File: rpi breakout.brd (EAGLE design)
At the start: 114 x 102.9 mm, 57 parts, among them IC1 PCA9505, J1 RASPBERRYPI-40-PIN-GPIO_PTH, U1 MAX11642EEG, U2 MAX11642EEG, U3 MAX11642EEG

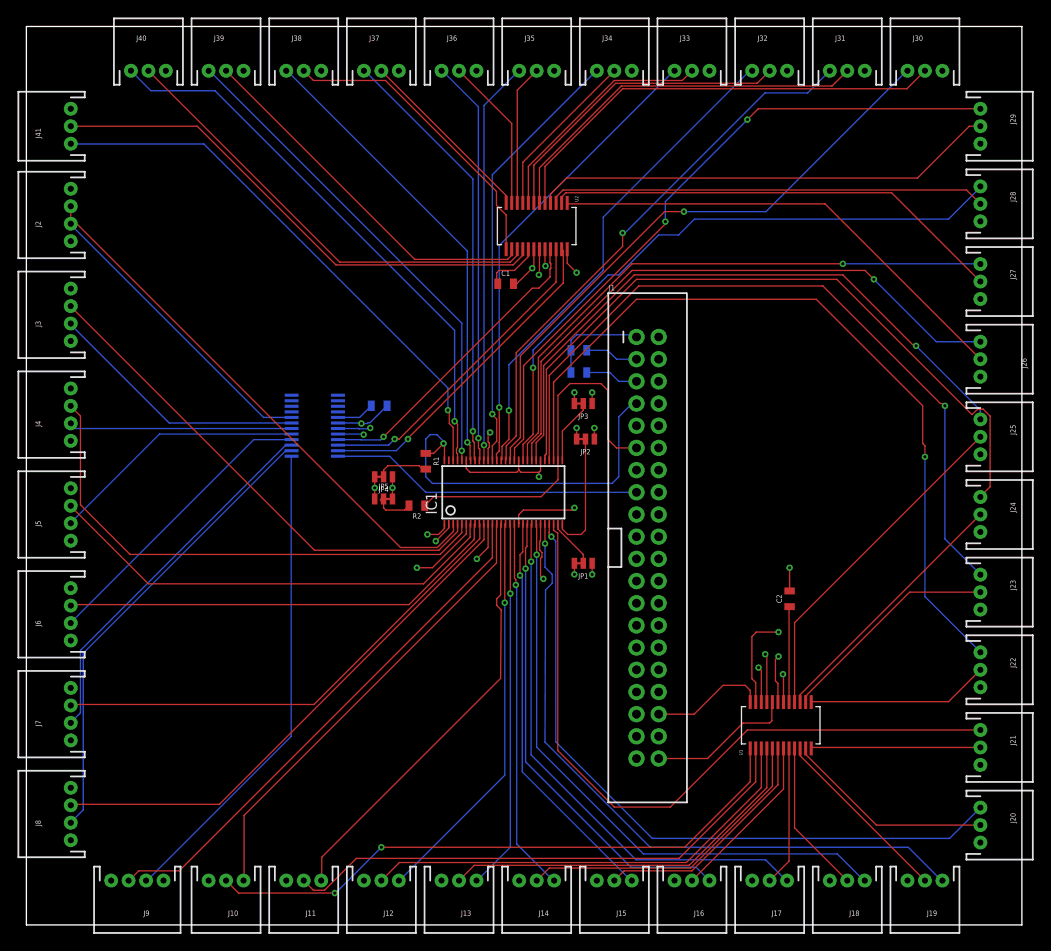
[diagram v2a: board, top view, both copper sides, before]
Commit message: updated silkscreen and increased trace sizes
increased sizes of all traces and update routing to clear DRC. Added silkscreen for all connections. Sent to fab
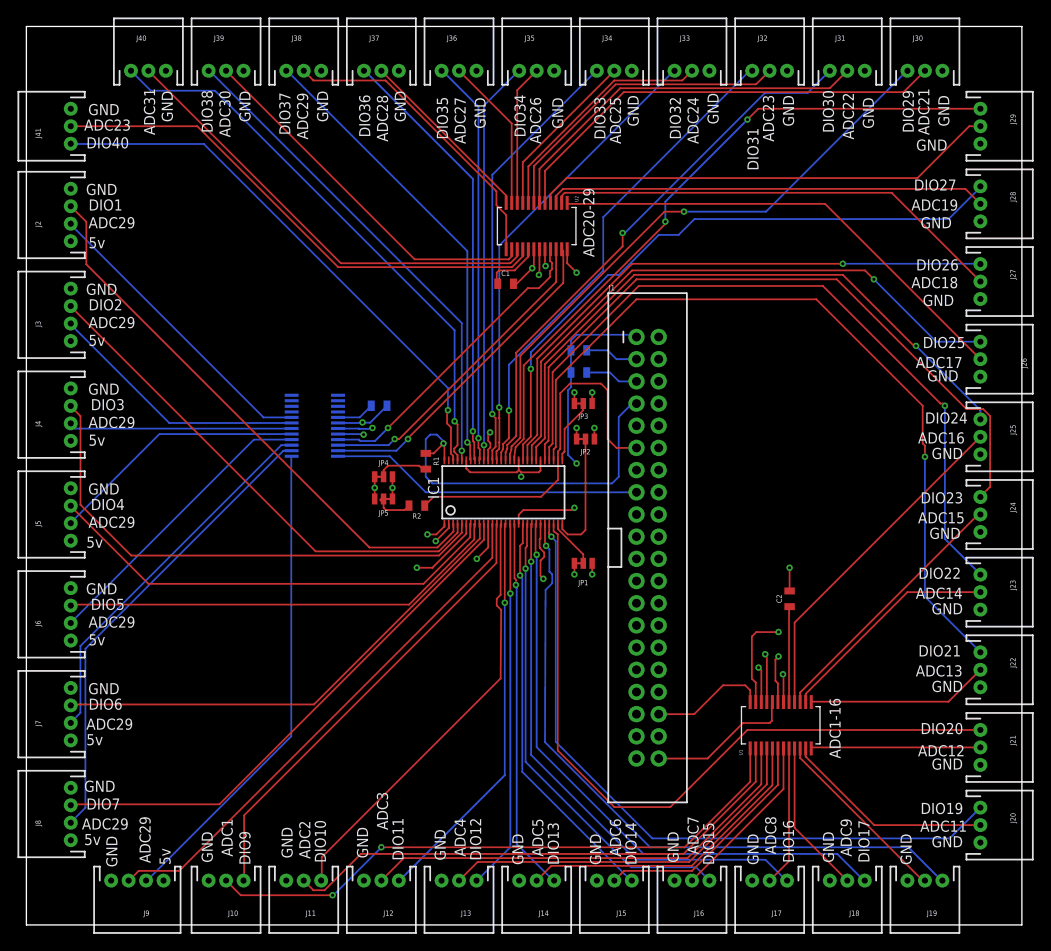
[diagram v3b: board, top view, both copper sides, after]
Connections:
- removed net 3.3V: J1.17
- net 3V: now also J1.17
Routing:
- net 3V: track 11.5 -> 31.8 mm, vias 0 -> 1
- net DIO1: track 62.4 -> 64.5 mm
- net DIO23: track 82.3 -> 81.8 mm
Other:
- board text added: "5v"
- board text added: "ADC1"
- board text added: "ADC1-16"
- board text added: "ADC11"
- board text added: "ADC12"
- board text added: "ADC13"
- board text added: "ADC14"
- board text added: "ADC15"
- board text added: "ADC16"
- board text added: "ADC17"
- board text added: "ADC18"
- board text added: "ADC19"
- board text added: "ADC2"
- board text added: "ADC20-29"
- board text added: "ADC21"
- board text added: "ADC22"
- board text added: "ADC23"
- board text added: "ADC24"
- board text added: "ADC25"
- board text added: "ADC26"
- board text added: "ADC27"
- board text added: "ADC28"
- board text added: "ADC29"
- board text added: "ADC3"
- board text added: "ADC30"
- board text added: "ADC31"
- board text added: "ADC33-39"
- board text added: "ADC4"
- board text added: "ADC5"
- board text added: "ADC6"
- board text added: "ADC7"
- board text added: "ADC8"
- board text added: "ADC9"
- board text added: "DIO1"
- board text added: "DIO10"
- board text added: "DIO11"
- board text added: "DIO12"
- board text added: "DIO13"
- board text added: "DIO14"
- board text added: "DIO15"
- board text added: "DIO16"
- board text added: "DIO17"
- board text added: "DIO19"
- board text added: "DIO2"
- board text added: "DIO20"
- board text added: "DIO21"
- board text added: "DIO22"
- board text added: "DIO23"
- board text added: "DIO24"
- board text added: "DIO25"
- board text added: "DIO26"
- board text added: "DIO27"
- board text added: "DIO29"
- board text added: "DIO3"
- board text added: "DIO30"
- board text added: "DIO31"
- board text added: "DIO32"
- board text added: "DIO33"
- board text added: "DIO34"
- board text added: "DIO35"
- board text added: "DIO36"
- board text added: "DIO37"
- board text added: "DIO38"
- board text added: "DIO4"
- board text added: "DIO40"
- board text added: "DIO5"
- board text added: "DIO6"
- board text added: "DIO7"
- board text added: "DIO9"
- board text added: "GND"
